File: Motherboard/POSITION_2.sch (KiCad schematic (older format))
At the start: 31 parts, among them Q10 MOSFET_N_(FDMA430NZ), Q11 MOSFET_P_(BS250FTA), Q8 MOSFET_N_(2N7002P,215), Q9 MOSFET_N_(2N7002P,215)

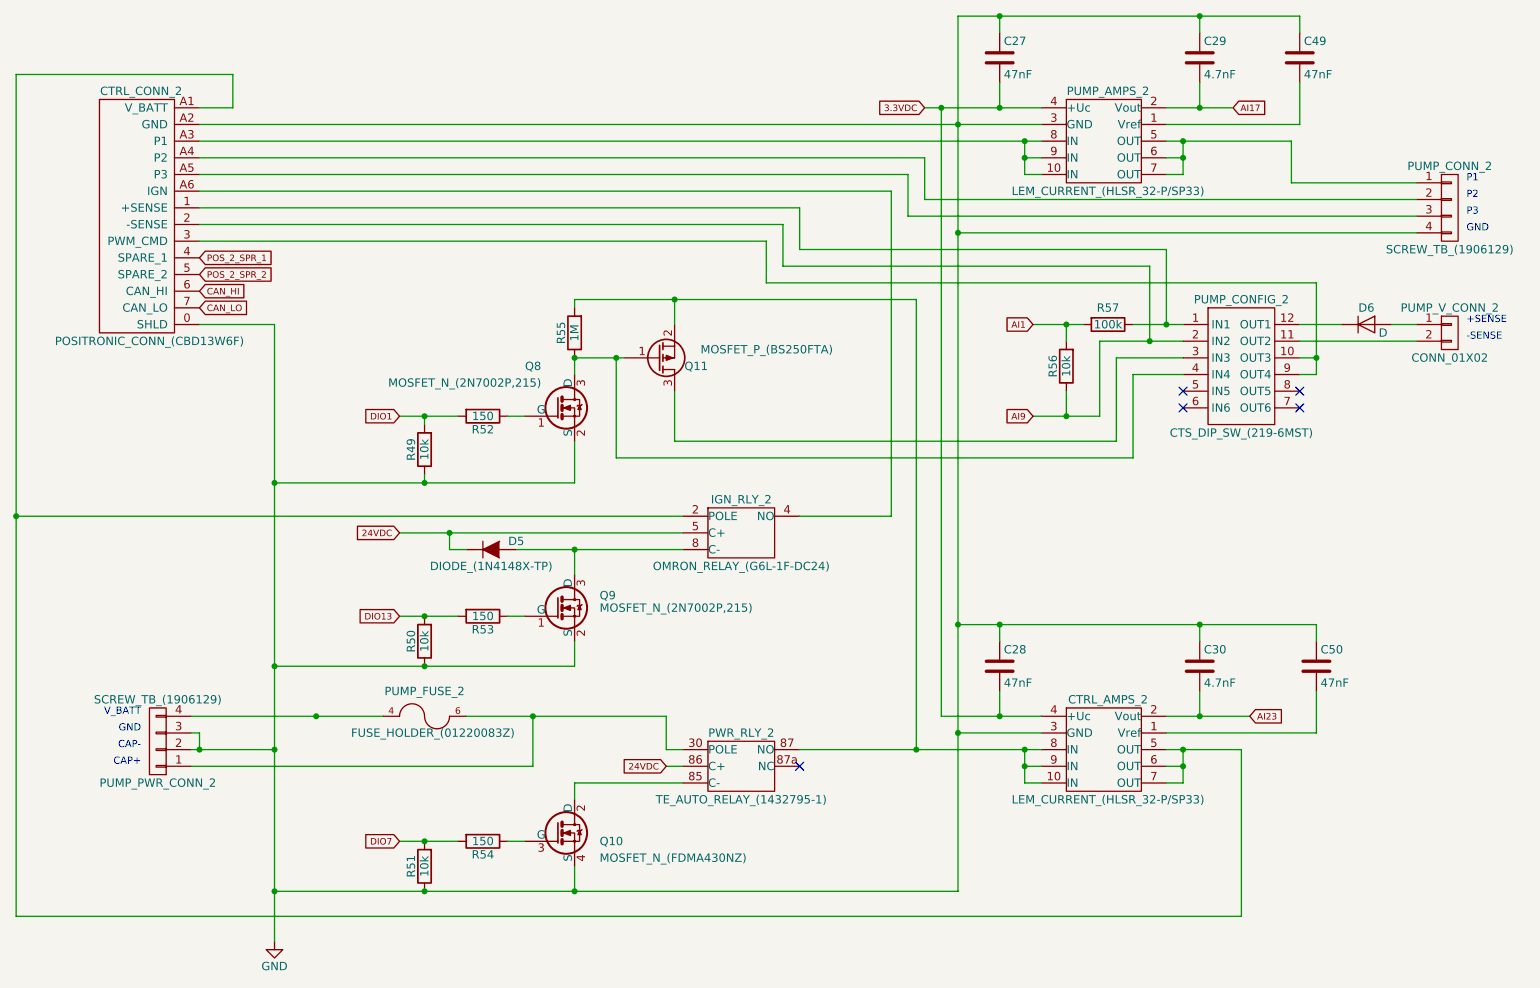
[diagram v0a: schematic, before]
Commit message: - Refer to Google Drive BOM for list of changes for v1.1 - Create drawing for Hella BLDC controller plate.
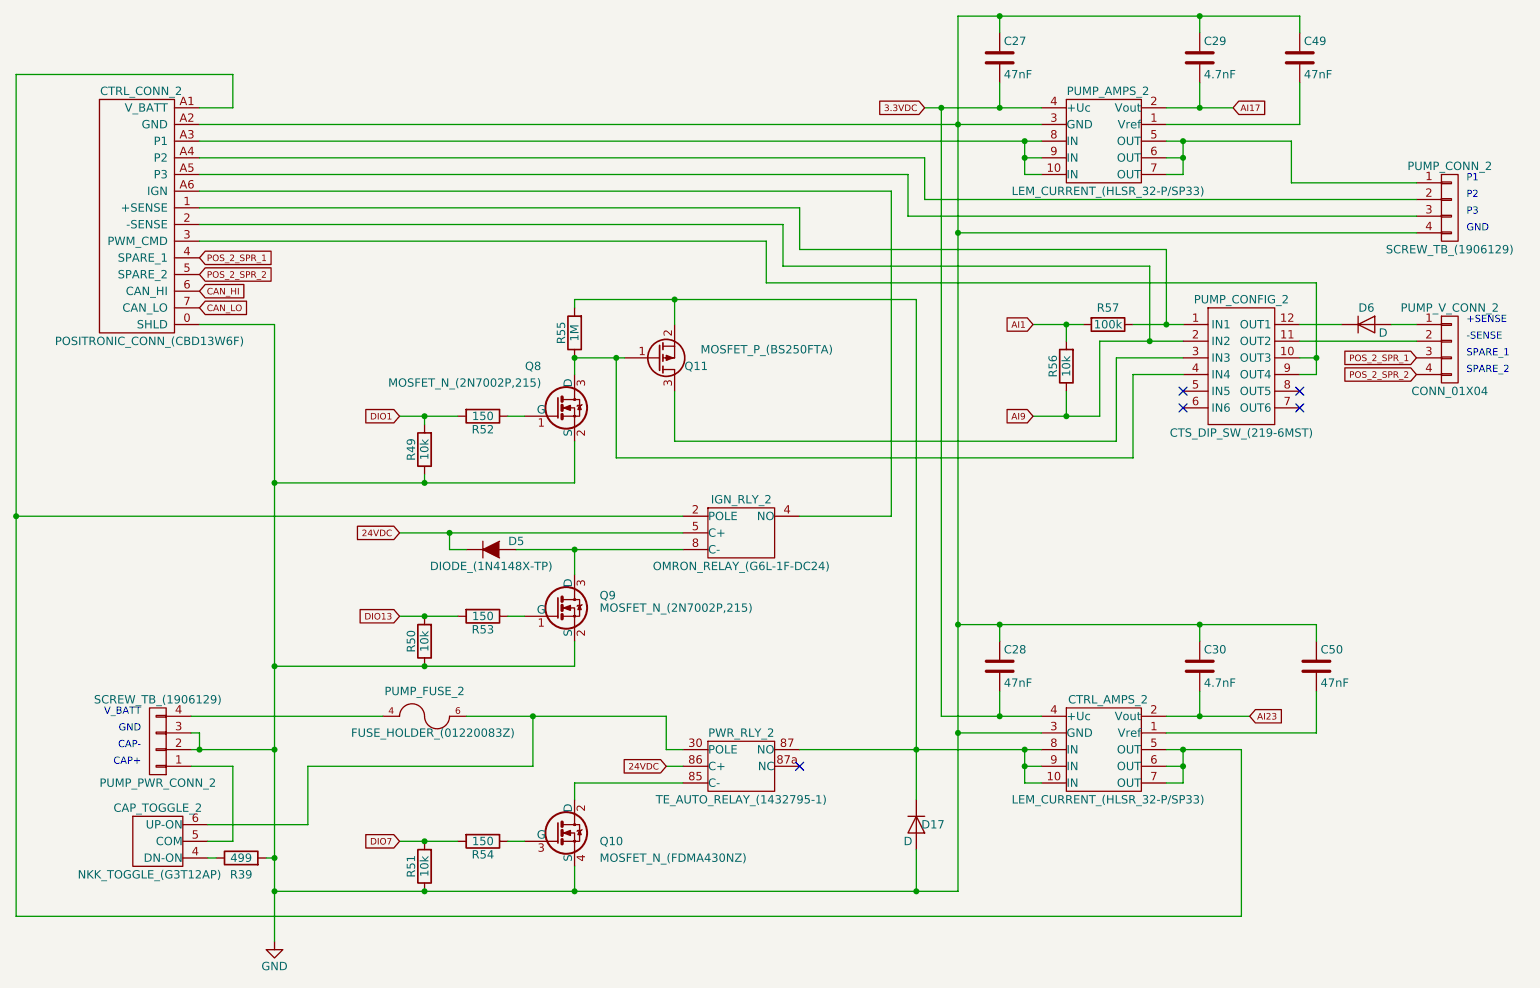
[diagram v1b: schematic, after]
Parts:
- removed PUMP_V_CONN_2: CONN_01X02, Smart_Tank:PHNX_TB_SCREW_2_POS_(1729128), symbol CONN_01X02
- added CAP_TOGGLE_2: NKK_TOGGLE_(G3T12AP), Smart_Tank:NKK_TOGGLE_(G3T12AP), symbol NKK_TOGGLE_(G3T12AP)
- added D17: D, Diodes_SMD:D_SOD-123, symbol D
- added PUMP_V_CONN_2: CONN_01X04, Smart_Tank:PHNX_TB_SCREW_4_POS_(1729144), symbol CONN_01X04
- added R39: 499, Resistors_SMD:R_1206, symbol R
- D6: footprint Diodes_SMD:SOD-523 -> Diodes_SMD:SOD-123
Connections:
- net GND: now also D17.2 (A), R39.2
- net POS_2_SPR_1: now also PUMP_V_CONN_2.3 (P3)
- net POS_2_SPR_2: now also PUMP_V_CONN_2.4 (P4)
- net at PUMP_FUSE_2.6, PUMP_FUSE_2.7, PWR_RLY_2.30 (POLE): now also CAP_TOGGLE_2.6 (UP-ON); no longer PUMP_PWR_CONN_2.1 (P1)
- net at CTRL_AMPS_2.10 (IN), CTRL_AMPS_2.8 (IN), CTRL_AMPS_2.9 (IN)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: now also D17.1 (K)
- net at PUMP_CONFIG_2.11 (OUT2): now also PUMP_V_CONN_2.2 (P2)
- net at D6.2 (A): now also PUMP_V_CONN_2.1 (P1)
- new net: CAP_TOGGLE_2.5 (COM), PUMP_PWR_CONN_2.1 (P1)
- new net: CAP_TOGGLE_2.4 (DN-ON), R39.1
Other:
- note added: "SPARE_1"
- note added: "SPARE_2"

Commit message: - Created Modbus Adapter.
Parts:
- C27, C28, C29, C30, C49, C50: symbol C -> Smart-Tank-Motherboard-rescue:C
- CAP_TOGGLE_2: symbol NKK_TOGGLE_(G3T12AP) -> Smart-Tank-Motherboard-rescue:NKK_TOGGLE_(G3T12AP)
- CTRL_AMPS_2, PUMP_AMPS_2: symbol LEM_CURRENT_(HLSR_32-P/SP33) -> Smart-Tank-Motherboard-rescue:LEM_CURRENT_(HLSR_32-P_SP33)
- CTRL_CONN_2: symbol POSITRONIC_CONN_(CBD13W6F) -> Smart-Tank-Motherboard-rescue:POSITRONIC_CONN_(CBD13W6F)
- D17, D6: symbol D -> Smart-Tank-Motherboard-rescue:D
- D5: symbol DIODE_(1N4148X-TP) -> Smart-Tank-Motherboard-rescue:DIODE_(1N4148X-TP)
- IGN_RLY_2: symbol OMRON_RELAY_(G6L-1F-DC24) -> Smart-Tank-Motherboard-rescue:OMRON_RELAY_(G6L-1F-DC24)
- PUMP_CONFIG_2: symbol CTS_DIP_SW_(219-6MST) -> Smart-Tank-Motherboard-rescue:CTS_DIP_SW_(219-6MST)
- PUMP_CONN_2, PUMP_PWR_CONN_2: symbol SCREW_TB_(1906129) -> Smart-Tank-Motherboard-rescue:SCREW_TB_(1906129)
- PUMP_FUSE_2: symbol FUSE_HOLDER_(01220083Z) -> Smart-Tank-Motherboard-rescue:FUSE_HOLDER_(01220083Z)
- PUMP_V_CONN_2: symbol CONN_01X04 -> Smart-Tank-Motherboard-rescue:CONN_01X04
- PWR_RLY_2: symbol TE_AUTO_RELAY_(1432795-1) -> Smart-Tank-Motherboard-rescue:TE_AUTO_RELAY_(1432795-1)
- Q10: symbol MOSFET_N_(FDMA430NZ) -> Smart-Tank-Motherboard-rescue:MOSFET_N_(FDMA430NZ)
- Q11: symbol MOSFET_P_(BS250FTA) -> Smart-Tank-Motherboard-rescue:MOSFET_P_(BS250FTA)
- Q8, Q9: symbol MOSFET_N_(2N7002P,215) -> Smart-Tank-Motherboard-rescue:MOSFET_N_(2N7002P,215)
- R39, R49, R50, R51, R52, R53, R54, R55, R56, R57: symbol R -> Smart-Tank-Motherboard-rescue:R
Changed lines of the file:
@@
-EESchema Schematic File Version 2
-LIBS:Smart Tank Motherboard-rescue
-LIBS:power
-LIBS:device
-LIBS:transistors
-LIBS:conn
-LIBS:linear
-LIBS:regul
-LIBS:74xx
-LIBS:cmos4000
-LIBS:adc-dac
-LIBS:memory
-LIBS:xilinx
-LIBS:microcontrollers
-LIBS:dsp
-LIBS:microchip
-LIBS:analog_switches
-LIBS:motorola
-LIBS:texas
-LIBS:intel
-LIBS:audio
-LIBS:interface
-LIBS:digital-audio
-LIBS:philips
-LIBS:display
-LIBS:cypress
-LIBS:siliconi
-LIBS:opto
-LIBS:atmel
-LIBS:contrib
-LIBS:valves
+EESchema Schematic File Version 4
 LIBS:Smart Tank Motherboard-cache
-EELAYER 25 0
+EELAYER 29 0
 EELAYER END
 $Descr A4 11693 8268
@@
 $EndDescr
 $Comp
-L R R54
+L Smart-Tank-Motherboard-rescue:R R54
 U 1 1 57A91D91
 P 4200 5750
@@
 $EndComp
 $Comp
-L R R51
+L Smart-Tank-Motherboard-rescue:R R51
 U 1 1 57A91D98
 P 3850 5900
@@
 $EndComp
 $Comp
-L SCREW_TB_(1906129) PUMP_PWR_CONN_2
+L Smart-Tank-Motherboard-rescue:SCREW_TB_(1906129) PUMP_PWR_CONN_2
 U 1 1 57A91DA0
 P 2250 5150
@@
 CAP+
 $Comp
-L GND #PWR023
+L Smart-Tank-Motherboard-rescue:GND #PWR023
 U 1 1 57A91DAB
 P 2950 6350
@@
 $EndComp
 $Comp
-L SCREW_TB_(1906129) PUMP_CONN_2
+L Smart-Tank-Motherboard-rescue:SCREW_TB_(1906129) PUMP_CONN_2
 U 1 1 57A91DC0
 P 10000 1950
@@
 GND
 $Comp
-L POSITRONIC_CONN_(CBD13W6F) CTRL_CONN_2
+L Smart-Tank-Motherboard-rescue:POSITRONIC_CONN_(CBD13W6F) CTRL_CONN_2
 U 1 1 57A91DCB
 P 2150 1900
@@
 $EndComp
 $Comp
-L MOSFET_N_(FDMA430NZ) Q10
+L Smart-Tank-Motherboard-rescue:MOSFET_N_(FDMA430NZ) Q10
 U 1 1 57A91DD9
 P 4650 5700
@@
 $EndComp
 $Comp
-L TE_AUTO_RELAY_(1432795-1) PWR_RLY_2
+L Smart-Tank-Motherboard-rescue:TE_AUTO_RELAY_(1432795-1) PWR_RLY_2
 U 1 1 57A91DE0
 P 5650 5400
@@
 AI23
 $Comp
-L OMRON_RELAY_(G6L-1F-DC24) IGN_RLY_2
+L Smart-Tank-Motherboard-rescue:OMRON_RELAY_(G6L-1F-DC24) IGN_RLY_2
 U 1 1 57A91DEC
 P 5650 4000
@@
 $EndComp
 $Comp
-L MOSFET_N_(2N7002P,215) Q9
+L Smart-Tank-Motherboard-rescue:MOSFET_N_(2N7002P,215) Q9
 U 1 1 57A91DF3
 P 4650 4350
@@
 $EndComp
 $Comp
-L R R53
+L Smart-Tank-Motherboard-rescue:R R53
 U 1 1 57A91DFA
 P 4200 4400
@@
 $EndComp
 $Comp
-L R R50
+L Smart-Tank-Motherboard-rescue:R R50
 U 1 1 57A91E01
 P 3850 4550
@@
 CAN_LO
 $Comp
-L DIODE_(1N4148X-TP) D5
+L Smart-Tank-Motherboard-rescue:DIODE_(1N4148X-TP) D5
 U 1 1 57A91E0C
 P 4250 4000
@@
 POS_2_SPR_2
 $Comp
-L MOSFET_N_(2N7002P,215) Q8
+L Smart-Tank-Motherboard-rescue:MOSFET_N_(2N7002P,215) Q8
 U 1 1 57A91E15
 P 4650 3150
@@
 $EndComp
 $Comp
-L MOSFET_P_(BS250FTA) Q11
+L Smart-Tank-Motherboard-rescue:MOSFET_P_(BS250FTA) Q11
 U 1 1 57A91E1C
 P 5250 2850
@@
 $EndComp
 $Comp
-L R R52
+L Smart-Tank-Motherboard-rescue:R R52
 U 1 1 57A91E23
 P 4200 3200
@@
 $EndComp
 $Comp
-L R R55
+L Smart-Tank-Motherboard-rescue:R R55
 U 1 1 57A91E2A
 P 4750 2700
@@
 DIO1
 $Comp
-L R R49
+L Smart-Tank-Motherboard-rescue:R R49
 U 1 1 57A91E32
 P 3850 3400
@@
 NoConn ~ 6100 5300
 $Comp
-L C C29
+L Smart-Tank-Motherboard-rescue:C C29
 U 1 1 57A91E54
 P 8500 1050
@@
 $EndComp
 $Comp
-L C C27
+L Smart-Tank-Motherboard-rescue:C C27
 U 1 1 57A91E5B
 P 7300 1050
@@
 $EndComp
 $Comp
-L C C30
+L Smart-Tank-Motherboard-rescue:C C30
 U 1 1 57A91E62
 P 8500 4700
@@
 $EndComp
 $Comp
-L C C28
+L Smart-Tank-Motherboard-rescue:C C28
 U 1 1 57A91E69
 P 7300 4700
@@
 $EndComp
 $Comp
-L CTS_DIP_SW_(219-6MST) PUMP_CONFIG_2
+L Smart-Tank-Motherboard-rescue:CTS_DIP_SW_(219-6MST) PUMP_CONFIG_2
 U 1 1 57A91E70
 P 8750 2900
@@
 NoConn ~ 8400 3150
 $Comp
-L R R56
+L Smart-Tank-Motherboard-rescue:R R56
 U 1 1 57A91E84
 P 7700 2900
@@
 $EndComp
 $Comp
-L R R57
+L Smart-Tank-Motherboard-rescue:R R57
 U 1 1 57A91E8B
 P 7950 2650
@@
 AI9
 $Comp
-L D D6
+L Smart-Tank-Motherboard-rescue:D D6
 U 1 1 57A91F2D
 P 9500 2650
@@
 $EndComp
 $Comp
-L FUSE_HOLDER_(01220083Z) PUMP_FUSE_2
+L Smart-Tank-Motherboard-rescue:FUSE_HOLDER_(01220083Z) PUMP_FUSE_2
 U 1 1 57A91DD2
 P 3850 5000
@@
 $EndComp
 $Comp
-L LEM_CURRENT_(HLSR_32-P/SP33) PUMP_AMPS_2
+L Smart-Tank-Motherboard-rescue:LEM_CURRENT_(HLSR_32-P_SP33) PUMP_AMPS_2
 U 1 1 57B742FB
 P 7800 1550
@@
 $EndComp
 $Comp
-L LEM_CURRENT_(HLSR_32-P/SP33) CTRL_AMPS_2
+L Smart-Tank-Motherboard-rescue:LEM_CURRENT_(HLSR_32-P_SP33) CTRL_AMPS_2
 U 1 1 57B76028
 P 7800 5200
@@
 $EndComp
 $Comp
-L C C49
+L Smart-Tank-Motherboard-rescue:C C49
 U 1 1 57D1DCED
 P 9100 1050
@@
 $EndComp
 $Comp
-L C C50
+L Smart-Tank-Motherboard-rescue:C C50
 U 1 1 57D1E27A
 P 9200 4700
@@
 Connection ~ 8500 4450
 $Comp
-L NKK_TOGGLE_(G3T12AP) CAP_TOGGLE_2
+L Smart-Tank-Motherboard-rescue:NKK_TOGGLE_(G3T12AP) CAP_TOGGLE_2
 U 1 1 59767FDC
 P 2250 5750
@@
 	3150 5300 4500 5300
 $Comp
-L D D17
+L Smart-Tank-Motherboard-rescue:D D17
 U 1 1 5976912A
 P 6800 5650
@@
 	2700 5300 2450 5300
 $Comp
-L R R39
+L Smart-Tank-Motherboard-rescue:R R39
 U 1 1 5978B008
 P 2750 5850
@@
 Connection ~ 2950 5850
 $Comp
-L CONN_01X04 PUMP_V_CONN_2
+L Smart-Tank-Motherboard-rescue:CONN_01X04 PUMP_V_CONN_2
 U 1 1 59797540
 P 10000 2800
